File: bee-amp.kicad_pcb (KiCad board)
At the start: 2 copper layers, 29 x 53.3 mm, 12 parts, among them J1 Conn_01x02_Male, J2 Conn_01x02_Male, J3 Conn_01x02_Male, J4 Conn_01x02_Male

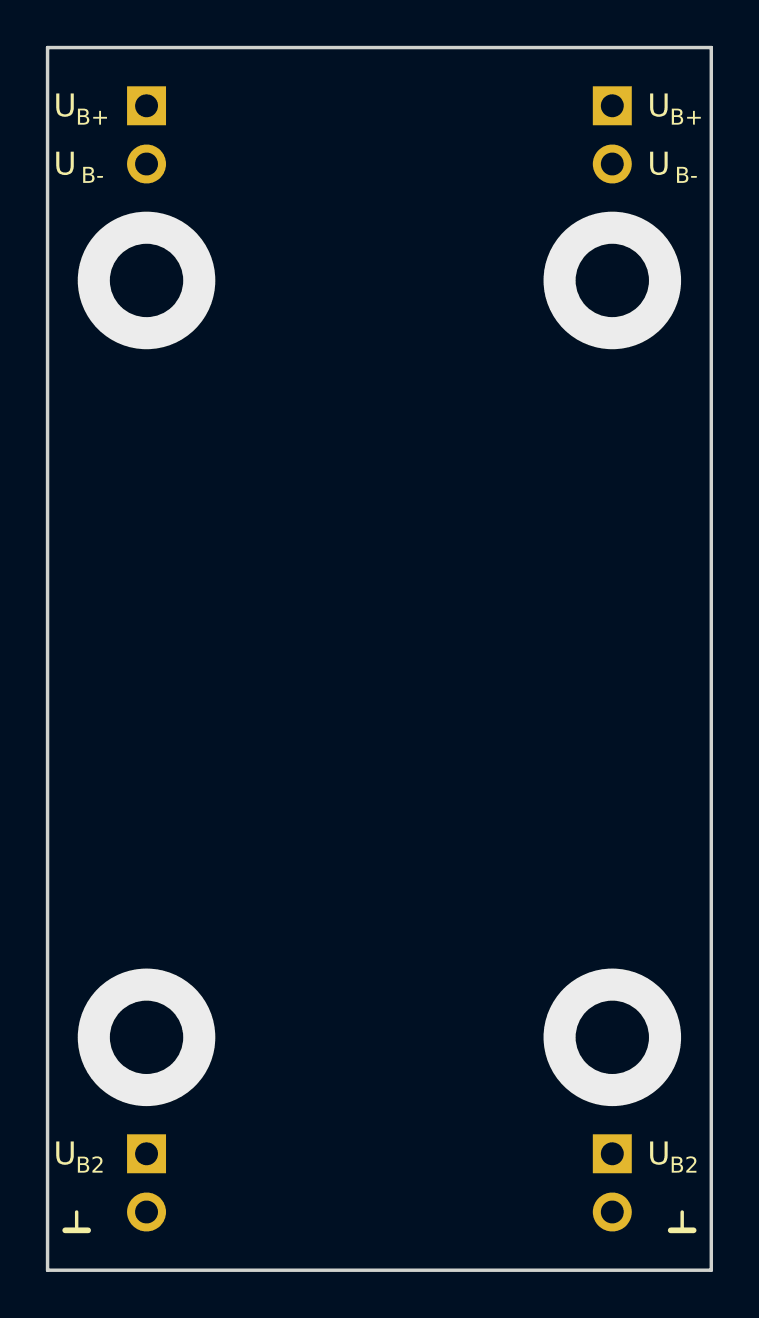
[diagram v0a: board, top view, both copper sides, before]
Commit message: schematic and basic layout
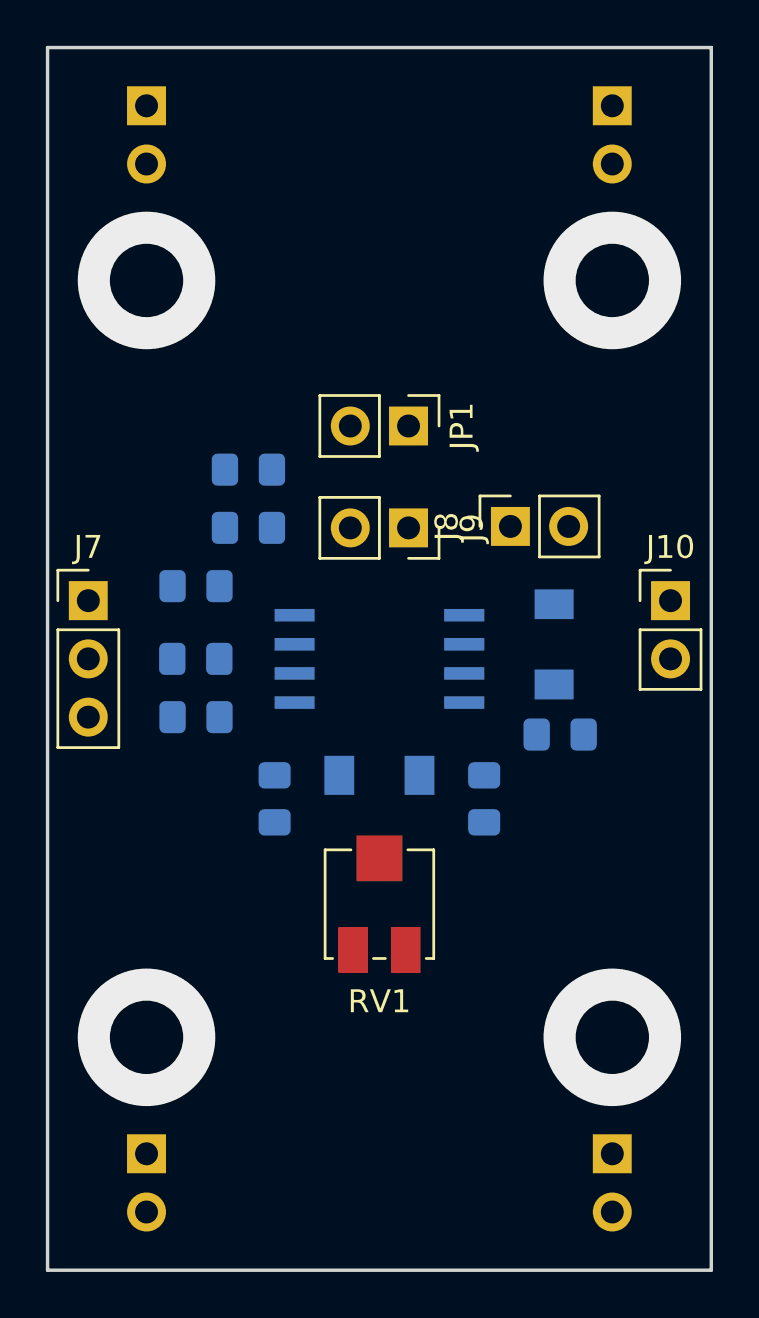
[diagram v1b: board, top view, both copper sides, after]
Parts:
- removed REF** (x2): Text_U_B+_Silkscreen, Symbol-emt:Text_U_B+_Silkscreen
- removed REF** (x2): Text_U_B-_Silkscreen, Symbol-emt:Text_U_B-_Silkscreen
- removed REF** (x2): Text_U_B2_Silkscreen, Symbol-emt:Text_U_B2_Silkscreen
- removed REF** (x2): Symbol_GND_Silkscreen, Symbol-emt:Symbol_GND_Silkscreen
- added C1: 0.1µF, Capacitor_SMD:C_0805_2012Metric_Pad1.15x1.40mm_HandSolder, B.Cu at (96.8, 118.9)
- added C2: 0.1µF, Capacitor_SMD:C_0805_2012Metric_Pad1.15x1.40mm_HandSolder, B.Cu at (80.9, 112.4)
- added D1: LL4148, Diode_SMD:D_MiniMELF, B.Cu at (88.9, 120.7)
- added D2: LL4148, Diode_SMD:D_MiniMELF, B.Cu at (96.5, 114.9)
- added J10: Conn_01x02, Connector_PinHeader_2.54mm:PinHeader_1x02_P2.54mm_Vertical, F.Cu at (101.6, 113.0)
- added J7: Conn_01x03, Connector_PinHeader_2.54mm:PinHeader_1x03_P2.54mm_Vertical, F.Cu at (76.2, 113.0)
- added J8: Conn_01x02, Connector_PinSocket_2.54mm:PinSocket_1x02_P2.54mm_Vertical, F.Cu at (94.6, 109.8)
- added J9: Conn_01x02, Connector_PinSocket_2.54mm:PinSocket_1x02_P2.54mm_Vertical, F.Cu at (90.2, 109.9)
- added JP1: Jumper, Connector_PinHeader_2.54mm:PinHeader_1x02_P2.54mm_Vertical, F.Cu at (90.2, 105.4)
- added R1: R, Resistor_SMD:R_0805_2012Metric_Pad1.15x1.40mm_HandSolder, B.Cu at (80.9, 118.1)
- added R2: R, Resistor_SMD:R_0805_2012Metric_Pad1.15x1.40mm_HandSolder, B.Cu at (80.9, 115.6)
- added R3: 0R, Resistor_SMD:R_0805_2012Metric_Pad1.15x1.40mm_HandSolder, B.Cu at (84.3, 121.7)
- added R4: 0R, Resistor_SMD:R_0805_2012Metric_Pad1.15x1.40mm_HandSolder, B.Cu at (93.5, 121.7)
- added R5: R, Resistor_SMD:R_0805_2012Metric_Pad1.15x1.40mm_HandSolder, B.Cu at (83.2, 107.3)
- added R6: R, Resistor_SMD:R_0805_2012Metric_Pad1.15x1.40mm_HandSolder, B.Cu at (83.2, 109.9)
- added RV1: 20k, Potentiometer_SMD:Potentiometer_Bourns_3314J_Vertical, F.Cu at (88.9, 126.3)
- added U1: OP07, Package_SO:SO-8_5.3x6.2mm_P1.27mm, B.Cu at (88.9, 115.6)
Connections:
- net +15V renamed V+
- net -15V renamed V-

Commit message: Update lables and mounting holes.
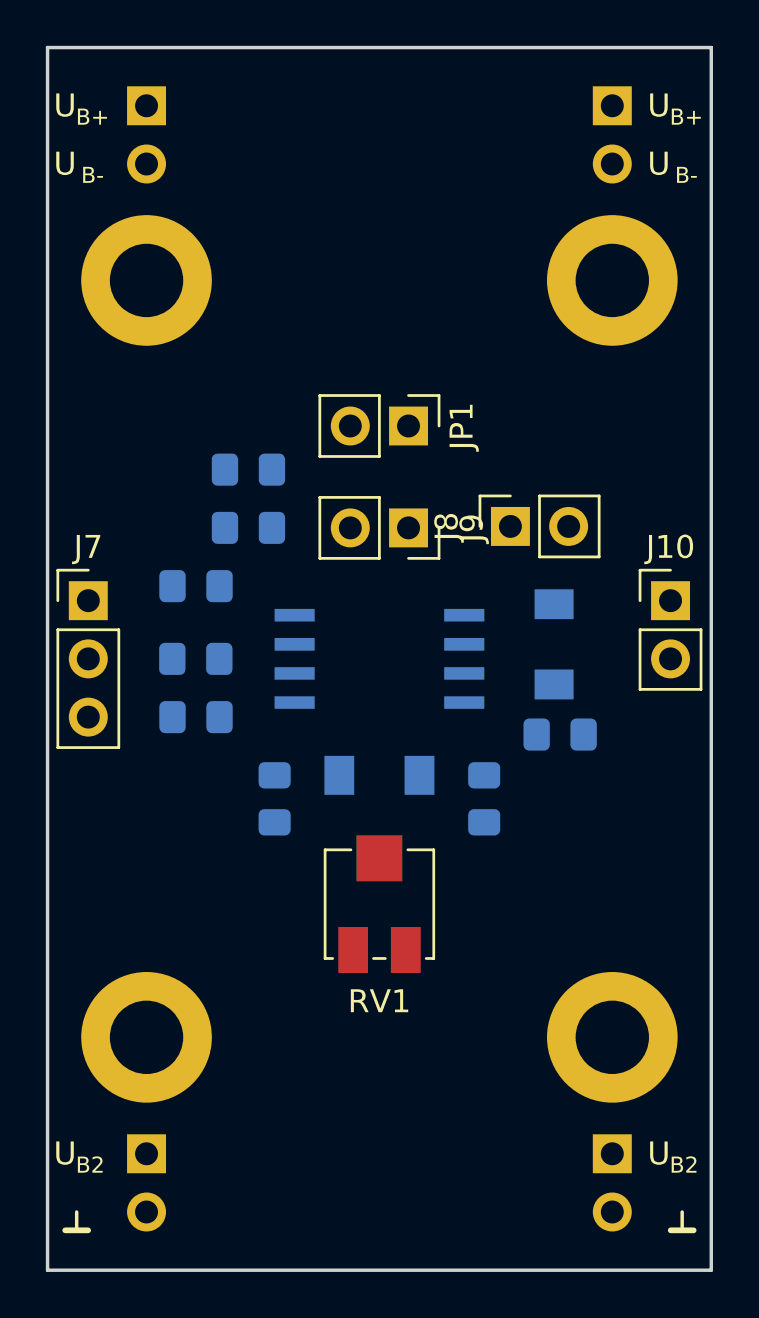
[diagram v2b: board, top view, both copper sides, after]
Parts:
- added H1: Silkscreen_Label, Symbol-emt:Text_U_B+_Silkscreen, F.Cu at (75.2, 91.4)
- added H10: MountingHole_Pad, MountingHole:MountingHole_3.2mm_M3_ISO7380_Pad, F.Cu at (99.1, 99.1)
- added H11: MountingHole_Pad, MountingHole:MountingHole_3.2mm_M3_ISO7380_Pad, F.Cu at (78.7, 132.1)
- added H12: MountingHole_Pad, MountingHole:MountingHole_3.2mm_M3_ISO7380_Pad, F.Cu at (99.1, 132.1)
- added H2: Silkscreen_Label, Symbol-emt:Text_U_B+_Silkscreen, F.Cu at (101.1, 91.4)
- added H3: Silkscreen_Label, Symbol-emt:Text_U_B-_Silkscreen, F.Cu at (101.1, 94.0)
- added H4: Silkscreen_Label, Symbol-emt:Text_U_B-_Silkscreen, F.Cu at (75.2, 94.0)
- added H5: Silkscreen_Label, Symbol-emt:Text_U_B2_Silkscreen, F.Cu at (75.2, 137.2)
- added H6: Silkscreen_Label, Symbol-emt:Text_U_B2_Silkscreen, F.Cu at (101.1, 137.2)
- added H7: Silkscreen_Label, Symbol-emt:Symbol_GND_Silkscreen, F.Cu at (75.7, 139.7)
- added H8: Silkscreen_Label, Symbol-emt:Symbol_GND_Silkscreen, F.Cu at (102.1, 139.7)
- added H9: MountingHole_Pad, MountingHole:MountingHole_3.2mm_M3_ISO7380_Pad, F.Cu at (78.7, 99.1)
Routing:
- net (no net): vias 4 -> 0
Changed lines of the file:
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@@
     (thickness 1.6)
     (drawings 4)
-    (tracks 4)
+    (tracks 0)
     (zones 0)
-    (modules 21)
+    (modules 33)
     (nets 16)
   )
@@
     (solder_mask_min_width 0.25)
     (aux_axis_origin 0 0)
-    (visible_elements 7FFFFFFF)
+    (visible_elements 7FFFF7FF)
     (pcbplotparams
       (layerselection 0x010fc_ffffffff)
@@
     )
   )
+  (module Symbol-emt:Text_U_B+_Silkscreen (layer F.Cu)
+    (at 75.184 91.44)
+    (descr "Voltage Label Betriebsspannung")
+    (tags "Voltage Label Betriebsspannung")
+    (attr virtual)
+    (fp_text reference H1 (at 0 1.65) (layer F.SilkS) hide
+      (effects (font (size 1 1) (thickness 0.15)))
+    )
+    (fp_text value Silkscreen_Label (at 0 -1.5) (layer F.Fab) hide
+      (effects (font (size 1 1) (thickness 0.15)))
+    )
+    (fp_text user B+ (at 1.2 0.5) (layer F.SilkS)
+      (effects (font (size 0.7 0.7) (thickness 0.1)))
+    )
+    (fp_text user U (at 0 0) (layer F.SilkS)
+      (effects (font (size 1 1) (thickness 0.15)))
+    )
+  )
+  (module Symbol-emt:Text_U_B+_Silkscreen (layer F.Cu)
+    (at 101.092 91.44)
+    (descr "Voltage Label Betriebsspannung")
+    (tags "Voltage Label Betriebsspannung")
+    (attr virtual)
+    (fp_text reference H2 (at 0 1.65) (layer F.SilkS) hide
+      (effects (font (size 1 1) (thickness 0.15)))
+    )
+    (fp_text value Silkscreen_Label (at 0 -1.5) (layer F.Fab) hide
+      (effects (font (size 1 1) (thickness 0.15)))
+    )
+    (fp_text user U (at 0 0) (layer F.SilkS)
+      (effects (font (size 1 1) (thickness 0.15)))
+    )
+    (fp_text user B+ (at 1.2 0.5) (layer F.SilkS)
+      (effects (font (size 0.7 0.7) (thickness 0.1)))
+    )
+  )
+  (module Symbol-emt:Text_U_B-_Silkscreen (layer F.Cu)
+    (at 101.092 93.98)
+    (descr "Voltage Label Betriebsspannung")
+    (tags "Voltage Label Betriebsspannung")
+    (attr virtual)
+    (fp_text reference H3 (at 0 1.65) (layer F.SilkS) hide
+      (effects (font (size 1 1) (thickness 0.15)))
+    )
+    (fp_text value Silkscreen_Label (at 0 -1.5) (layer F.Fab) hide
+      (effects (font (size 1 1) (thickness 0.15)))
+    )
+    (fp_text user U (at 0 0) (layer F.SilkS)
+      (effects (font (size 1 1) (thickness 0.15)))
+    )
+    (fp_text user B- (at 1.2 0.5) (layer F.SilkS)
+      (effects (font (size 0.7 0.7) (thickness 0.1)))
+    )
+  )
+  (module Symbol-emt:Text_U_B-_Silkscreen (layer F.Cu)
+    (at 75.184 93.98)
+    (descr "Voltage Label Betriebsspannung")
+    (tags "Voltage Label Betriebsspannung")
+    (attr virtual)
+    (fp_text reference H4 (at 0 1.65) (layer F.SilkS) hide
+      (effects (font (size 1 1) (thickness 0.15)))
+    )
+    (fp_text value Silkscreen_Label (at 0 -1.5) (layer F.Fab) hide
+      (effects (font (size 1 1) (thickness 0.15)))
+    )
+    (fp_text user B- (at 1.2 0.5) (layer F.SilkS)
+      (effects (font (size 0.7 0.7) (thickness 0.1)))
+    )
+    (fp_text user U (at 0 0) (layer F.SilkS)
+      (effects (font (size 1 1) (thickness 0.15)))
+    )
+  )
+  (module Symbol-emt:Text_U_B2_Silkscreen (layer F.Cu)
+    (at 75.184 137.16)
+    (descr "Voltage Label Betriebsspannung")
+    (tags "Voltage Label Betriebsspannung")
+    (attr virtual)
+    (fp_text reference H5 (at 0 1.65) (layer F.SilkS) hide
+      (effects (font (size 1 1) (thickness 0.15)))
+    )
+    (fp_text value Silkscreen_Label (at 0 -1.5) (layer F.Fab) hide
+      (effects (font (size 1 1) (thickness 0.15)))
+    )
+    (fp_text user U (at 0 0) (layer F.SilkS)
+      (effects (font (size 1 1) (thickness 0.15)))
+    )
+    (fp_text user B2 (at 1.1 0.5) (layer F.SilkS)
+      (effects (font (size 0.7 0.7) (thickness 0.1)))
+    )
+  )
+  (module Symbol-emt:Text_U_B2_Silkscreen (layer F.Cu)
+    (at 101.092 137.16)
+    (descr "Voltage Label Betriebsspannung")
+    (tags "Voltage Label Betriebsspannung")
+    (attr virtual)
+    (fp_text reference H6 (at 0 1.65) (layer F.SilkS) hide
+      (effects (font (size 1 1) (thickness 0.15)))
+    )
+    (fp_text value Silkscreen_Label (at 0 -1.5) (layer F.Fab) hide
+      (effects (font (size 1 1) (thickness 0.15)))
+    )
+    (fp_text user B2 (at 1.1 0.5) (layer F.SilkS)
+      (effects (font (size 0.7 0.7) (thickness 0.1)))
+    )
+    (fp_text user U (at 0 0) (layer F.SilkS)
+      (effects (font (size 1 1) (thickness 0.15)))
+    )
+  )
+  (module Symbol-emt:Symbol_GND_Silkscreen (layer F.Cu)
+    (at 75.692 139.7)
+    (descr "Symbol GND")
+    (tags "Symbol GND")
+    (attr virtual)
+    (fp_text reference H7 (at 0 1.6) (layer F.SilkS) hide
+      (effects (font (size 1 1) (thickness 0.15)))
+    )
+    (fp_text value Silkscreen_Label (at 0 -0.75) (layer F.Fab) hide
+      (effects (font (size 1 1) (thickness 0.15)))
+    )
+    (fp_line (start 0 0.8) (end 0 0) (layer F.SilkS) (width 0.15))
+    (fp_line (start -0.5 0.8) (end 0.5 0.8) (layer F.SilkS) (width 0.25))
+  )
+  (module Symbol-emt:Symbol_GND_Silkscreen (layer F.Cu)
+    (at 102.108 139.7)
+    (descr "Symbol GND")
+    (tags "Symbol GND")
+    (attr virtual)
+    (fp_text reference H8 (at 0 1.6) (layer F.SilkS) hide
+      (effects (font (size 1 1) (thickness 0.15)))
+    )
+    (fp_text value Silkscreen_Label (at 0 -0.75) (layer F.Fab) hide
+      (effects (font (size 1 1) (thickness 0.15)))
+    )
+    (fp_line (start -0.5 0.8) (end 0.5 0.8) (layer F.SilkS) (width 0.25))
+    (fp_line (start 0 0.8) (end 0 0) (layer F.SilkS) (width 0.15))
+  )
+  (module MountingHole:MountingHole_3.2mm_M3_ISO7380_Pad locked (layer F.Cu)
+    (at 78.74 99.06)
+    (descr "Mounting Hole 3.2mm, M3, ISO7380")
+    (tags "mounting hole 3.2mm m3 iso7380")
+    (attr virtual)
+    (fp_text reference H9 (at 0 -3.85) (layer F.SilkS) hide
+      (effects (font (size 1 1) (thickness 0.15)))
+    )
+    (fp_text value MountingHole_Pad (at 0 3.85) (layer F.Fab)
+      (effects (font (size 1 1) (thickness 0.15)))
+    )
+    (fp_text user %R (at 0.3 0) (layer F.Fab)
+      (effects (font (size 1 1) (thickness 0.15)))
+    )
+    (fp_circle (center 0 0) (end 2.85 0) (layer Cmts.User) (width 0.15))
+    (fp_circle (center 0 0) (end 3.1 0) (layer F.CrtYd) (width 0.05))
+    (pad 1 thru_hole circle (at 0 0) (size 5.7 5.7) (drill 3.2) (layers *.Cu *.Mask)
+      (net 1 GND))
+  )
+  (module MountingHole:MountingHole_3.2mm_M3_ISO7380_Pad locked (layer F.Cu)
+    (at 99.06 99.06)
+    (descr "Mounting Hole 3.2mm, M3, ISO7380")
+    (tags "mounting hole 3.2mm m3 iso7380")
+    (attr virtual)
+    (fp_text reference H10 (at 0 -3.85) (layer F.SilkS) hide
+      (effects (font (size 1 1) (thickness 0.15)))
+    )
+    (fp_text value MountingHole_Pad (at 0 3.85) (layer F.Fab)
+      (effects (font (size 1 1) (thickness 0.15)))
+    )
+    (fp_circle (center 0 0) (end 3.1 0) (layer F.CrtYd) (width 0.05))
+    (fp_circle (center 0 0) (end 2.85 0) (layer Cmts.User) (width 0.15))
+    (fp_text user %R (at 0.3 0) (layer F.Fab)
+      (effects (font (size 1 1) (thickness 0.15)))
+    )
+    (pad 1 thru_hole circle (at 0 0) (size 5.7 5.7) (drill 3.2) (layers *.Cu *.Mask)
+      (net 1 GND))
+  )
+  (module MountingHole:MountingHole_3.2mm_M3_ISO7380_Pad locked (layer F.Cu)
+    (at 78.74 132.08)
+    (descr "Mounting Hole 3.2mm, M3, ISO7380")
+    (tags "mounting hole 3.2mm m3 iso7380")
+    (attr virtual)
+    (fp_text reference H11 (at 0 -3.85) (layer F.SilkS) hide
+      (effects (font (size 1 1) (thickness 0.15)))
+    )
+    (fp_text value MountingHole_Pad (at 0 3.85) (layer F.Fab)
+      (effects (font (size 1 1) (thickness 0.15)))
+    )
+    (fp_text user %R (at 0.3 0) (layer F.Fab)
+      (effects (font (size 1 1) (thickness 0.15)))
+    )
+    (fp_circle (center 0 0) (end 2.85 0) (layer Cmts.User) (width 0.15))
+    (fp_circle (center 0 0) (end 3.1 0) (layer F.CrtYd) (width 0.05))
+    (pad 1 thru_hole circle (at 0 0) (size 5.7 5.7) (drill 3.2) (layers *.Cu *.Mask)
+      (net 1 GND))
+  )
+  (module MountingHole:MountingHole_3.2mm_M3_ISO7380_Pad locked (layer F.Cu)
+    (at 99.06 132.08)
+    (descr "Mounting Hole 3.2mm, M3, ISO7380")
+    (tags "mounting hole 3.2mm m3 iso7380")
+    (attr virtual)
+    (fp_text reference H12 (at 0 -3.85) (layer F.SilkS) hide
+      (effects (font (size 1 1) (thickness 0.15)))
+    )
+    (fp_text value MountingHole_Pad (at 0 3.85) (layer F.Fab)
+      (effects (font (size 1 1) (thickness 0.15)))
+    )
+    (fp_circle (center 0 0) (end 3.1 0) (layer F.CrtYd) (width 0.05))
+    (fp_circle (center 0 0) (end 2.85 0) (layer Cmts.User) (width 0.15))
+    (fp_text user %R (at 0.3 0) (layer F.Fab)
+      (effects (font (size 1 1) (thickness 0.15)))
+    )
+    (pad 1 thru_hole circle (at 0 0) (size 5.7 5.7) (drill 3.2) (layers *.Cu *.Mask)
+      (net 1 GND))
+  )
   (gr_line (start 103.378 88.9) (end 103.378 142.24) (layer Edge.Cuts) (width 0.15))
   (gr_line (start 74.422 142.24) (end 103.378 142.24) (layer Edge.Cuts) (width 0.15))
   (gr_line (start 74.422 88.9) (end 103.378 88.9) (layer Edge.Cuts) (width 0.15))
   (gr_line (start 74.422 88.9) (end 74.422 142.24) (layer Edge.Cuts) (width 0.15))
-  (via (at 78.74 99.06) (size 6) (drill 3.2) (layers F.Cu B.Cu) (net 0) (status 40000))
-  (via (at 99.06 99.06) (size 6) (drill 3.2) (layers F.Cu B.Cu) (net 0) (status 40000))
-  (via (at 99.06 132.08) (size 6) (drill 3.2) (layers F.Cu B.Cu) (net 0) (status 40000))
-  (via (at 78.74 132.08) (size 6) (drill 3.2) (layers F.Cu B.Cu) (net 0) (status 40000))
 )

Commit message: Layout traces.
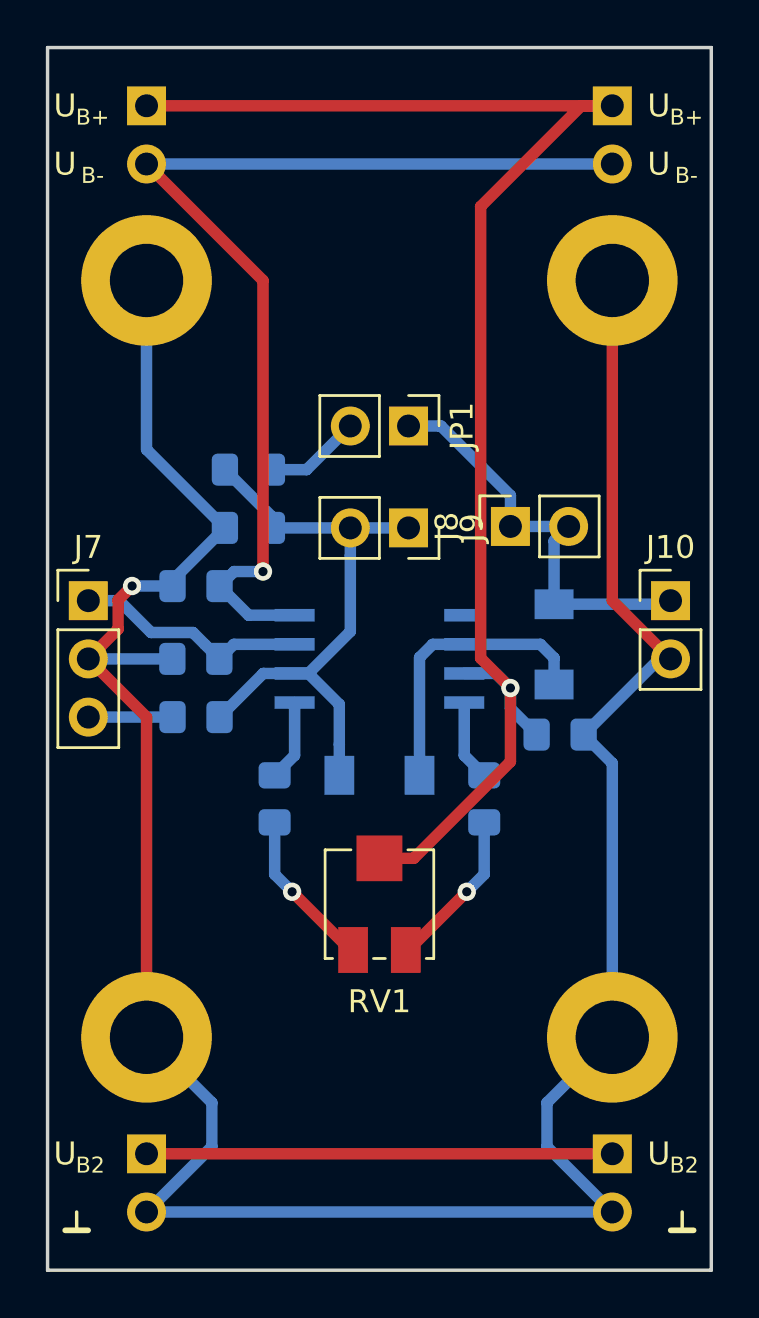
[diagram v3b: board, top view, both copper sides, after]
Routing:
- net GND: track 0.00 -> 119.4 mm, vias 0 -> 1
- net V+: track 0.00 -> 64.9 mm, vias 0 -> 1
- net V-: track 0.00 -> 46.2 mm, vias 0 -> 1
- net Net-(D1-Pad2): track 0.00 -> 26.1 mm
- net +5V: track 0.00 -> 20.3 mm
- net Net-(D2-Pad1): track 0.00 -> 18.4 mm
- net Net-(D1-Pad1): track 0.00 -> 12.6 mm
- net Net-(J7-Pad1): track 0.00 -> 10.3 mm
- net Net-(R4-Pad2): track 0.00 -> 7.06 mm, vias 0 -> 1
- net Net-(R3-Pad1): track 0.00 -> 7.06 mm, vias 0 -> 1
- net Net-(JP1-Pad2): track 0.00 -> 4.21 mm
- net Net-(J7-Pad3): track 0.00 -> 3.67 mm
- net V_OS_2: track 0.00 -> 3.54 mm
- net V_OS_1: track 0.00 -> 3.54 mm
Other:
- net class Default: trace_width 0.25 -> 0.5
